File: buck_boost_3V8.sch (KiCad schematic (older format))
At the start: 10 parts

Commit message: Finally finished final draft
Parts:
- C10: renamed from C?; value 10 pF -> 10pF
- C11: renamed from C?; value 4.7 nF -> 4.7nF
- C12, C8, C9: renamed from C?; value 10 uF -> 10uF
- L1: renamed from L?; value 1.5 uH -> 1.5uH
- R1: renamed from R?; value 100 k -> 100k
- R2: renamed from R?; value 681 k -> 681k
- R3: renamed from R?; value 182 k -> 182k
- gave numbers to parts that had none: 1
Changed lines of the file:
@@
 $Descr A4 11693 8268
 encoding utf-8
-Sheet 4 6
+Sheet 3 6
 Title ""
 Date ""
@@
 AR Path="/60C5D7FB" Ref="IC?"  Part="1"
 AR Path="/60BA4931/60C5D7FB" Ref="IC?"  Part="1"
-AR Path="/60BA4931/60C52C6F/60C5D7FB" Ref="IC?"  Part="1"
-F 0 "IC?" H 5300 4215 50  0000 C CNN
+AR Path="/60BA4931/60C52C6F/60C5D7FB" Ref="IC1"  Part="1"
+F 0 "IC1" H 5300 4215 50  0000 C CNN
 F 1 "TPS63050YFFR" H 5300 4124 50  0000 C CNN
 F 2 "BGA12C40P3X4_129X169X62" H 4850 2900 50  0001 L CNN
@@
 AR Path="/60C5D804" Ref="L?"  Part="1"
 AR Path="/60BA4931/60C5D804" Ref="L?"  Part="1"
-AR Path="/60BA4931/60C52C6F/60C5D804" Ref="L?"  Part="1"
-F 0 "L?" V 5490 2750 50  0000 C CNN
-F 1 "1.5 uH" V 5399 2750 50  0000 C CNN
+AR Path="/60BA4931/60C52C6F/60C5D804" Ref="L1"  Part="1"
+F 0 "L1" V 5490 2750 50  0000 C CNN
+F 1 "1.5uH" V 5399 2750 50  0000 C CNN
 F 2 "" H 5300 2750 50  0001 C CNN
 F 3 "~" H 5300 2750 50  0001 C CNN
@@
 AR Path="/60C5D812" Ref="R?"  Part="1"
 AR Path="/60BA4931/60C5D812" Ref="R?"  Part="1"
-AR Path="/60BA4931/60C52C6F/60C5D812" Ref="R?"  Part="1"
-F 0 "R?" H 6468 3596 50  0000 L CNN
-F 1 "681 k" H 6468 3505 50  0000 L CNN
+AR Path="/60BA4931/60C52C6F/60C5D812" Ref="R2"  Part="1"
+F 0 "R2" H 6468 3596 50  0000 L CNN
+F 1 "681k" H 6468 3505 50  0000 L CNN
 F 2 "" V 6440 3540 50  0001 C CNN
 F 3 "~" H 6400 3550 50  0001 C CNN
@@
 AR Path="/60C5D81C" Ref="R?"  Part="1"
 AR Path="/60BA4931/60C5D81C" Ref="R?"  Part="1"
-AR Path="/60BA4931/60C52C6F/60C5D81C" Ref="R?"  Part="1"
-F 0 "R?" H 6468 3996 50  0000 L CNN
-F 1 "182 k" H 6468 3905 50  0000 L CNN
+AR Path="/60BA4931/60C52C6F/60C5D81C" Ref="R3"  Part="1"
+F 0 "R3" H 6468 3996 50  0000 L CNN
+F 1 "182k" H 6468 3905 50  0000 L CNN
 F 2 "" V 6440 3940 50  0001 C CNN
 F 3 "~" H 6400 3950 50  0001 C CNN
@@
 AR Path="/60C5D82E" Ref="R?"  Part="1"
 AR Path="/60BA4931/60C5D82E" Ref="R?"  Part="1"
-AR Path="/60BA4931/60C52C6F/60C5D82E" Ref="R?"  Part="1"
-F 0 "R?" H 7368 3846 50  0000 L CNN
-F 1 "100 k" H 7368 3755 50  0000 L CNN
+AR Path="/60BA4931/60C52C6F/60C5D82E" Ref="R1"  Part="1"
+F 0 "R1" H 7368 3846 50  0000 L CNN
+F 1 "100k" H 7368 3755 50  0000 L CNN
 F 2 "" V 7340 3790 50  0001 C CNN
 F 3 "~" H 7300 3800 50  0001 C CNN
@@
 AR Path="/60C5D83A" Ref="C?"  Part="1"
 AR Path="/60BA4931/60C5D83A" Ref="C?"  Part="1"
-AR Path="/60BA4931/60C52C6F/60C5D83A" Ref="C?"  Part="1"
-F 0 "C?" H 7815 4196 50  0000 L CNN
-F 1 "10 uF" H 7815 4105 50  0000 L CNN
+AR Path="/60BA4931/60C52C6F/60C5D83A" Ref="C9"  Part="1"
+F 0 "C9" H 7815 4196 50  0000 L CNN
+F 1 "10uF" H 7815 4105 50  0000 L CNN
 F 2 "" H 7738 4000 50  0001 C CNN
 F 3 "~" H 7700 4150 50  0001 C CNN
@@
 AR Path="/60C5D844" Ref="C?"  Part="1"
 AR Path="/60BA4931/60C5D844" Ref="C?"  Part="1"
-AR Path="/60BA4931/60C52C6F/60C5D844" Ref="C?"  Part="1"
-F 0 "C?" H 8315 4196 50  0000 L CNN
-F 1 "10 uF" H 8315 4105 50  0000 L CNN
+AR Path="/60BA4931/60C52C6F/60C5D844" Ref="C8"  Part="1"
+F 0 "C8" H 8315 4196 50  0000 L CNN
+F 1 "10uF" H 8315 4105 50  0000 L CNN
 F 2 "" H 8238 4000 50  0001 C CNN
 F 3 "~" H 8200 4150 50  0001 C CNN
@@
 AR Path="/60C5D862" Ref="C?"  Part="1"
 AR Path="/60BA4931/60C5D862" Ref="C?"  Part="1"
-AR Path="/60BA4931/60C52C6F/60C5D862" Ref="C?"  Part="1"
-F 0 "C?" H 4615 4346 50  0000 L CNN
-F 1 "4.7 nF" H 4615 4255 50  0000 L CNN
+AR Path="/60BA4931/60C52C6F/60C5D862" Ref="C11"  Part="1"
+F 0 "C11" H 4615 4346 50  0000 L CNN
+F 1 "4.7nF" H 4615 4255 50  0000 L CNN
 F 2 "" H 4538 4150 50  0001 C CNN
 F 3 "~" H 4500 4300 50  0001 C CNN
@@
 AR Path="/60C5D86C" Ref="C?"  Part="1"
 AR Path="/60BA4931/60C5D86C" Ref="C?"  Part="1"
-AR Path="/60BA4931/60C52C6F/60C5D86C" Ref="C?"  Part="1"
-F 0 "C?" H 4115 3846 50  0000 L CNN
-F 1 "10 uF" H 4115 3755 50  0000 L CNN
+AR Path="/60BA4931/60C52C6F/60C5D86C" Ref="C12"  Part="1"
+F 0 "C12" H 4115 3846 50  0000 L CNN
+F 1 "10uF" H 4115 3755 50  0000 L CNN
 F 2 "" H 4038 3650 50  0001 C CNN
 F 3 "~" H 4000 3800 50  0001 C CNN
@@
 AR Path="/60C5D87D" Ref="C?"  Part="1"
 AR Path="/60BA4931/60C5D87D" Ref="C?"  Part="1"
-AR Path="/60BA4931/60C52C6F/60C5D87D" Ref="C?"  Part="1"
-F 0 "C?" H 7015 3996 50  0000 L CNN
-F 1 "10 pF" H 7015 3905 50  0000 L CNN
+AR Path="/60BA4931/60C52C6F/60C5D87D" Ref="C10"  Part="1"
+F 0 "C10" H 7015 3996 50  0000 L CNN
+F 1 "10pF" H 7015 3905 50  0000 L CNN
 F 2 "" H 6938 3800 50  0001 C CNN
 F 3 "~" H 6900 3950 50  0001 C CNN

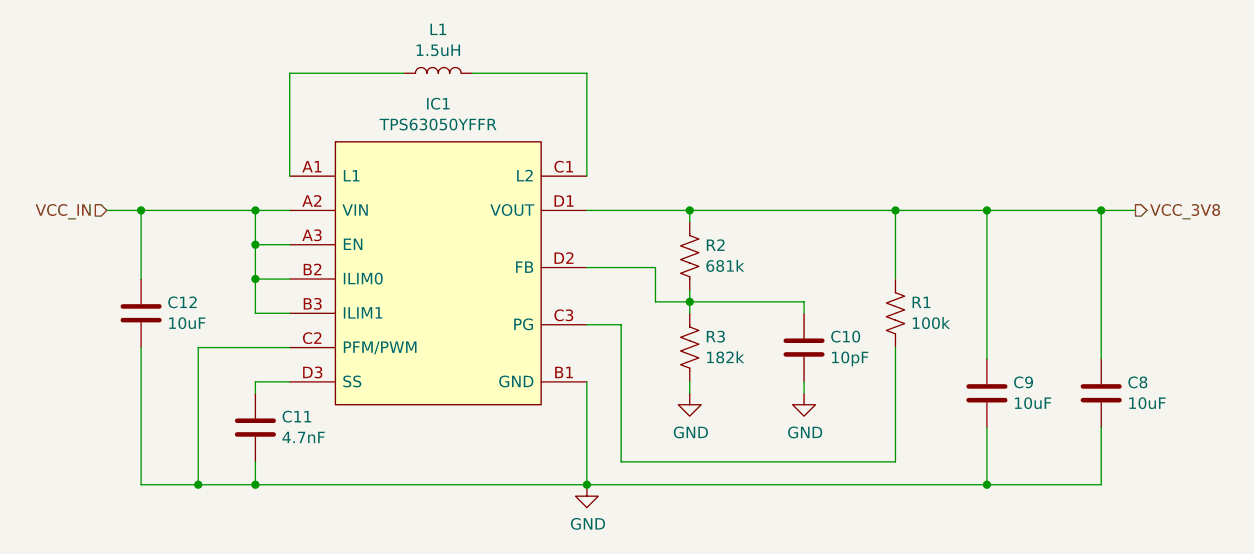
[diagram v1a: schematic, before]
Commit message: Fixed some symbols, assigned some footprints, and made wire labels
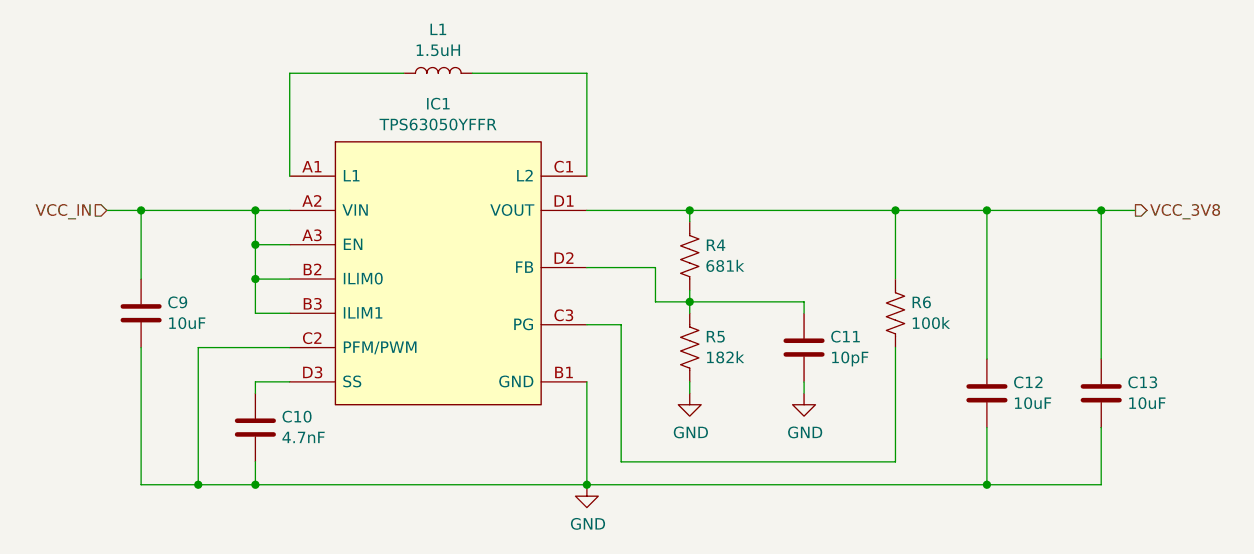
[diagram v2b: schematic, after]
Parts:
- IC1: footprint BGA12C40P3X4_129X169X62 -> Buck_Boost_IC:BGA12C40P3X4_129X169X62
- renumbered C11 to C10, C10 to C11, C9 to C12, C8 to C13, C12 to C9, R2 to R4, R3 to R5, R1 to R6
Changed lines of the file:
@@
 F 0 "IC1" H 5300 4215 50  0000 C CNN
 F 1 "TPS63050YFFR" H 5300 4124 50  0000 C CNN
-F 2 "BGA12C40P3X4_129X169X62" H 4850 2900 50  0001 L CNN
+F 2 "Buck_Boost_IC:BGA12C40P3X4_129X169X62" H 4850 2900 50  0001 L CNN
 F 3 "http://www.ti.com/lit/ds/symlink/tps63050.pdf" H 4850 2800 50  0001 L CNN
 F 4 "TPS6305x Single Inductor Buck-Boost with 1-A Switches and Adjustable Soft Start" H 4850 2700 50  0001 L CNN "Description"
@@
 AR Path="/60C5D812" Ref="R?"  Part="1"
 AR Path="/60BA4931/60C5D812" Ref="R?"  Part="1"
-AR Path="/60BA4931/60C52C6F/60C5D812" Ref="R2"  Part="1"
-F 0 "R2" H 6468 3596 50  0000 L CNN
+AR Path="/60BA4931/60C52C6F/60C5D812" Ref="R4"  Part="1"
+F 0 "R4" H 6468 3596 50  0000 L CNN
 F 1 "681k" H 6468 3505 50  0000 L CNN
 F 2 "" V 6440 3540 50  0001 C CNN
@@
 AR Path="/60C5D81C" Ref="R?"  Part="1"
 AR Path="/60BA4931/60C5D81C" Ref="R?"  Part="1"
-AR Path="/60BA4931/60C52C6F/60C5D81C" Ref="R3"  Part="1"
-F 0 "R3" H 6468 3996 50  0000 L CNN
+AR Path="/60BA4931/60C52C6F/60C5D81C" Ref="R5"  Part="1"
+F 0 "R5" H 6468 3996 50  0000 L CNN
 F 1 "182k" H 6468 3905 50  0000 L CNN
 F 2 "" V 6440 3940 50  0001 C CNN
@@
 AR Path="/60C5D823" Ref="#PWR?"  Part="1"
 AR Path="/60BA4931/60C5D823" Ref="#PWR?"  Part="1"
-AR Path="/60BA4931/60C52C6F/60C5D823" Ref="#PWR?"  Part="1"
-F 0 "#PWR?" H 6400 3900 50  0001 C CNN
+AR Path="/60BA4931/60C52C6F/60C5D823" Ref="#PWR017"  Part="1"
+F 0 "#PWR017" H 6400 3900 50  0001 C CNN
 F 1 "GND" H 6405 3977 50  0000 C CNN
 F 2 "" H 6400 4150 50  0001 C CNN
@@
 AR Path="/60C5D82E" Ref="R?"  Part="1"
 AR Path="/60BA4931/60C5D82E" Ref="R?"  Part="1"
-AR Path="/60BA4931/60C52C6F/60C5D82E" Ref="R1"  Part="1"
-F 0 "R1" H 7368 3846 50  0000 L CNN
+AR Path="/60BA4931/60C52C6F/60C5D82E" Ref="R6"  Part="1"
+F 0 "R6" H 7368 3846 50  0000 L CNN
 F 1 "100k" H 7368 3755 50  0000 L CNN
 F 2 "" V 7340 3790 50  0001 C CNN
@@
 AR Path="/60C5D83A" Ref="C?"  Part="1"
 AR Path="/60BA4931/60C5D83A" Ref="C?"  Part="1"
-AR Path="/60BA4931/60C52C6F/60C5D83A" Ref="C9"  Part="1"
-F 0 "C9" H 7815 4196 50  0000 L CNN
+AR Path="/60BA4931/60C52C6F/60C5D83A" Ref="C12"  Part="1"
+F 0 "C12" H 7815 4196 50  0000 L CNN
 F 1 "10uF" H 7815 4105 50  0000 L CNN
 F 2 "" H 7738 4000 50  0001 C CNN
@@
 AR Path="/60C5D844" Ref="C?"  Part="1"
 AR Path="/60BA4931/60C5D844" Ref="C?"  Part="1"
-AR Path="/60BA4931/60C52C6F/60C5D844" Ref="C8"  Part="1"
-F 0 "C8" H 8315 4196 50  0000 L CNN
+AR Path="/60BA4931/60C52C6F/60C5D844" Ref="C13"  Part="1"
+F 0 "C13" H 8315 4196 50  0000 L CNN
 F 1 "10uF" H 8315 4105 50  0000 L CNN
 F 2 "" H 8238 4000 50  0001 C CNN
@@
 AR Path="/60C5D862" Ref="C?"  Part="1"
 AR Path="/60BA4931/60C5D862" Ref="C?"  Part="1"
-AR Path="/60BA4931/60C52C6F/60C5D862" Ref="C11"  Part="1"
-F 0 "C11" H 4615 4346 50  0000 L CNN
+AR Path="/60BA4931/60C52C6F/60C5D862" Ref="C10"  Part="1"
+F 0 "C10" H 4615 4346 50  0000 L CNN
 F 1 "4.7nF" H 4615 4255 50  0000 L CNN
 F 2 "" H 4538 4150 50  0001 C CNN
@@
 AR Path="/60C5D86C" Ref="C?"  Part="1"
 AR Path="/60BA4931/60C5D86C" Ref="C?"  Part="1"
-AR Path="/60BA4931/60C52C6F/60C5D86C" Ref="C12"  Part="1"
-F 0 "C12" H 4115 3846 50  0000 L CNN
+AR Path="/60BA4931/60C52C6F/60C5D86C" Ref="C9"  Part="1"
+F 0 "C9" H 4115 3846 50  0000 L CNN
 F 1 "10uF" H 4115 3755 50  0000 L CNN
 F 2 "" H 4038 3650 50  0001 C CNN
@@
 AR Path="/60C5D877" Ref="#PWR?"  Part="1"
 AR Path="/60BA4931/60C5D877" Ref="#PWR?"  Part="1"
-AR Path="/60BA4931/60C52C6F/60C5D877" Ref="#PWR?"  Part="1"
-F 0 "#PWR?" H 6900 3900 50  0001 C CNN
+AR Path="/60BA4931/60C52C6F/60C5D877" Ref="#PWR018"  Part="1"
+F 0 "#PWR018" H 6900 3900 50  0001 C CNN
 F 1 "GND" H 6905 3977 50  0000 C CNN
 F 2 "" H 6900 4150 50  0001 C CNN
@@
 AR Path="/60C5D87D" Ref="C?"  Part="1"
 AR Path="/60BA4931/60C5D87D" Ref="C?"  Part="1"
-AR Path="/60BA4931/60C52C6F/60C5D87D" Ref="C10"  Part="1"
-F 0 "C10" H 7015 3996 50  0000 L CNN
+AR Path="/60BA4931/60C52C6F/60C5D87D" Ref="C11"  Part="1"
+F 0 "C11" H 7015 3996 50  0000 L CNN
 F 1 "10pF" H 7015 3905 50  0000 L CNN
 F 2 "" H 6938 3800 50  0001 C CNN
@@
 AR Path="/60C5D884" Ref="#PWR?"  Part="1"
 AR Path="/60BA4931/60C5D884" Ref="#PWR?"  Part="1"
-AR Path="/60BA4931/60C52C6F/60C5D884" Ref="#PWR?"  Part="1"
-F 0 "#PWR?" H 5950 4300 50  0001 C CNN
+AR Path="/60BA4931/60C52C6F/60C5D884" Ref="#PWR016"  Part="1"
+F 0 "#PWR016" H 5950 4300 50  0001 C CNN
 F 1 "GND" H 5955 4377 50  0000 C CNN
 F 2 "" H 5950 4550 50  0001 C CNN

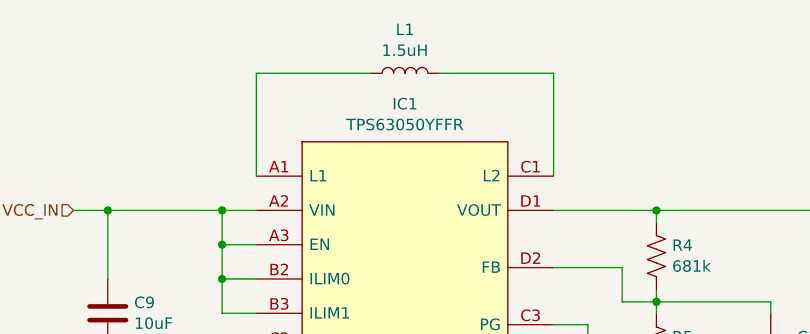
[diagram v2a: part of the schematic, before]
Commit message: Chose more parts and added more footprints. Have some resistors and all the capacitors to go
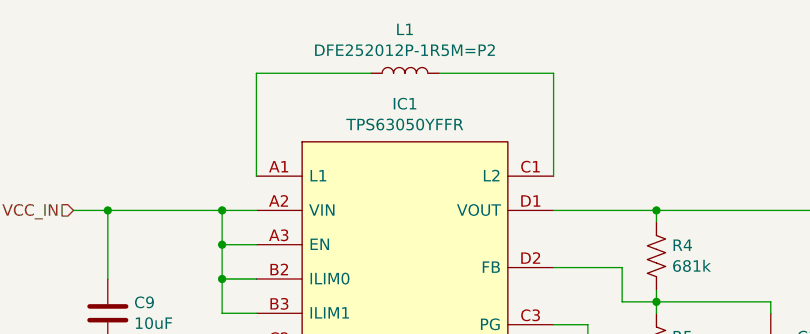
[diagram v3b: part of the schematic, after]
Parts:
- removed L1: 1.5uH, symbol Device:L
- added L1: DFE252012P-1R5M=P2, Inductor_SMD:DFE2HCAH1R0MJ0L, symbol Inductor_1v5uH:DFE252012P-1R5M=P2
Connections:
- net at IC1.A1 (L1): now also L1.1
- net at IC1.C1 (L2): now also L1.2
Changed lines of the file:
@@
 Wire Wire Line
 	5950 2750 5950 3200
-$Comp
-L Device:L L?
-U 1 1 60C5D804
-P 5300 2750
-AR Path="/60C5D804" Ref="L?"  Part="1"
-AR Path="/60BA4931/60C5D804" Ref="L?"  Part="1"
-AR Path="/60BA4931/60C52C6F/60C5D804" Ref="L1"  Part="1"
-F 0 "L1" V 5490 2750 50  0000 C CNN
-F 1 "1.5uH" V 5399 2750 50  0000 C CNN
-F 2 "" H 5300 2750 50  0001 C CNN
-F 3 "~" H 5300 2750 50  0001 C CNN
-	1    5300 2750
-	0    -1   -1   0
-$EndComp
 Wire Wire Line
 	5450 2750 5950 2750
@@
 Text HLabel 3850 3350 0    50   Input ~ 0
 VCC_IN
+$Comp
+L Inductor_1v5uH:DFE252012P-1R5M=P2 L1
+U 1 1 607595A6
+P 5300 2750
+F 0 "L1" H 5300 2940 50  0000 C CNN
+F 1 "DFE252012P-1R5M=P2" H 5300 2849 50  0000 C CNN
+F 2 "Inductor_SMD:DFE2HCAH1R0MJ0L" H 4950 2550 50  0001 L CNN
+F 3 "https://psearch.en.murata.com/inductor/product/DFE252012P-1R5M%23.html" H 4950 2450 50  0001 L CNN
+F 4 "Toko DFE252012P Series Shielded Wire-wound SMD Inductor with a Powered Iron Core, 1.5 uH Wire-Wound 3.9A Idc" H 4950 2350 50  0001 L CNN "Description"
+F 5 "1.2" H 4950 2250 50  0001 L CNN "Height"
+F 6 "Murata Electronics" H 4950 2150 50  0001 L CNN "Manufacturer_Name"
+F 7 "DFE252012P-1R5M=P2" H 4950 2050 50  0001 L CNN "Manufacturer_Part_Number"
+F 8 "81-DFE252012P-1R5MP2" H 4950 1950 50  0001 L CNN "Mouser Part Number"
+F 9 "https://www.mouser.co.uk/ProductDetail/Murata-Electronics/DFE252012P-1R5M%3dP2?qs=KuGPmAKtFKVOutr53B1A3A%3D%3D" H 4950 1850 50  0001 L CNN "Mouser Price/Stock"
+F 10 "DFE252012P-1R5M=P2" H 4950 1750 50  0001 L CNN "Arrow Part Number"
+F 11 "https://www.arrow.com/en/products/dfe252012p-1r5mp2/murata-manufacturing" H 4950 1650 50  0001 L CNN "Arrow Price/Stock"
+	1    5300 2750
+	1    0    0    -1
+$EndComp
 $EndSCHEMATC

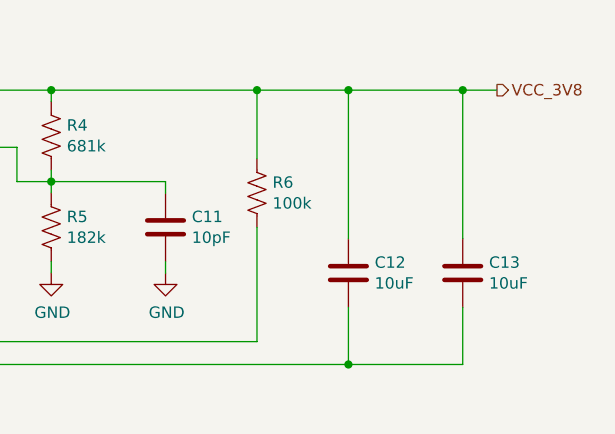
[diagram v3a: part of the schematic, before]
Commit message: Finished assigning footprints, and generated netlist
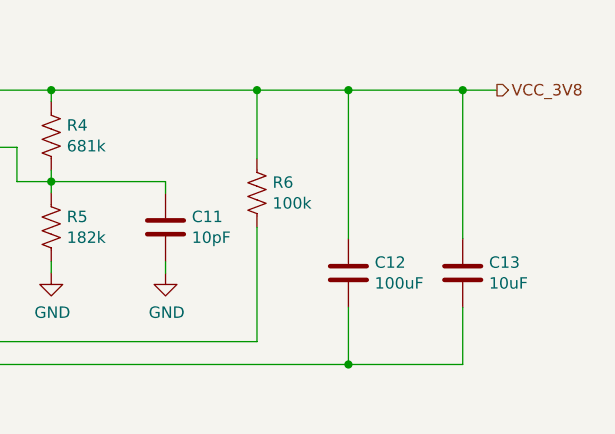
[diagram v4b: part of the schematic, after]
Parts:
- C10, C11: footprint (none) -> Capacitor_SMD:C_0603_1608Metric
- C12: value 10uF -> 100uF; footprint (none) -> Capacitor_SMD:C_1210_3225Metric
- C13, C9: footprint (none) -> Capacitor_SMD:C_0805_2012Metric
- R4: footprint (none) -> Resistor_SMD:R_1206_3216Metric
- R5, R6: footprint (none) -> Resistor_SMD:R_0603_1608Metric
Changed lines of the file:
@@
 F 0 "R4" H 6468 3596 50  0000 L CNN
 F 1 "681k" H 6468 3505 50  0000 L CNN
-F 2 "" V 6440 3540 50  0001 C CNN
+F 2 "Resistor_SMD:R_1206_3216Metric" V 6440 3540 50  0001 C CNN
 F 3 "~" H 6400 3550 50  0001 C CNN
 	1    6400 3550
@@
 F 0 "R5" H 6468 3996 50  0000 L CNN
 F 1 "182k" H 6468 3905 50  0000 L CNN
-F 2 "" V 6440 3940 50  0001 C CNN
+F 2 "Resistor_SMD:R_0603_1608Metric" V 6440 3940 50  0001 C CNN
 F 3 "~" H 6400 3950 50  0001 C CNN
 	1    6400 3950
@@
 F 0 "R6" H 7368 3846 50  0000 L CNN
 F 1 "100k" H 7368 3755 50  0000 L CNN
-F 2 "" V 7340 3790 50  0001 C CNN
+F 2 "Resistor_SMD:R_0603_1608Metric" V 7340 3790 50  0001 C CNN
 F 3 "~" H 7300 3800 50  0001 C CNN
 	1    7300 3800
@@
 AR Path="/60BA4931/60C52C6F/60C5D83A" Ref="C12"  Part="1"
 F 0 "C12" H 7815 4196 50  0000 L CNN
-F 1 "10uF" H 7815 4105 50  0000 L CNN
-F 2 "" H 7738 4000 50  0001 C CNN
+F 1 "100uF" H 7815 4105 50  0000 L CNN
+F 2 "Capacitor_SMD:C_1210_3225Metric" H 7738 4000 50  0001 C CNN
 F 3 "~" H 7700 4150 50  0001 C CNN
 	1    7700 4150
@@
 F 0 "C13" H 8315 4196 50  0000 L CNN
 F 1 "10uF" H 8315 4105 50  0000 L CNN
-F 2 "" H 8238 4000 50  0001 C CNN
+F 2 "Capacitor_SMD:C_0805_2012Metric" H 8238 4000 50  0001 C CNN
 F 3 "~" H 8200 4150 50  0001 C CNN
 	1    8200 4150
@@
 F 0 "C10" H 4615 4346 50  0000 L CNN
 F 1 "4.7nF" H 4615 4255 50  0000 L CNN
-F 2 "" H 4538 4150 50  0001 C CNN
+F 2 "Capacitor_SMD:C_0603_1608Metric" H 4538 4150 50  0001 C CNN
 F 3 "~" H 4500 4300 50  0001 C CNN
 	1    4500 4300
@@
 F 0 "C9" H 4115 3846 50  0000 L CNN
 F 1 "10uF" H 4115 3755 50  0000 L CNN
-F 2 "" H 4038 3650 50  0001 C CNN
+F 2 "Capacitor_SMD:C_0805_2012Metric" H 4038 3650 50  0001 C CNN
 F 3 "~" H 4000 3800 50  0001 C CNN
 	1    4000 3800
@@
 F 0 "C11" H 7015 3996 50  0000 L CNN
 F 1 "10pF" H 7015 3905 50  0000 L CNN
-F 2 "" H 6938 3800 50  0001 C CNN
+F 2 "Capacitor_SMD:C_0603_1608Metric" H 6938 3800 50  0001 C CNN
 F 3 "~" H 6900 3950 50  0001 C CNN
 	1    6900 3950
